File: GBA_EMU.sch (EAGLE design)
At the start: 83 parts, among them J1 USB-MINIB-5PIN, J2 AVR_SPI, SW1 LEFT, SW2 RIGHT, SW3 PWR_SWITCH, U1 MIC7221, U2 MICROCHIP_MCP1642B-ADJ, U4 LM4875, U5 Mic5365-2.8Y, U7 AZV321, X2 HEADPHONE

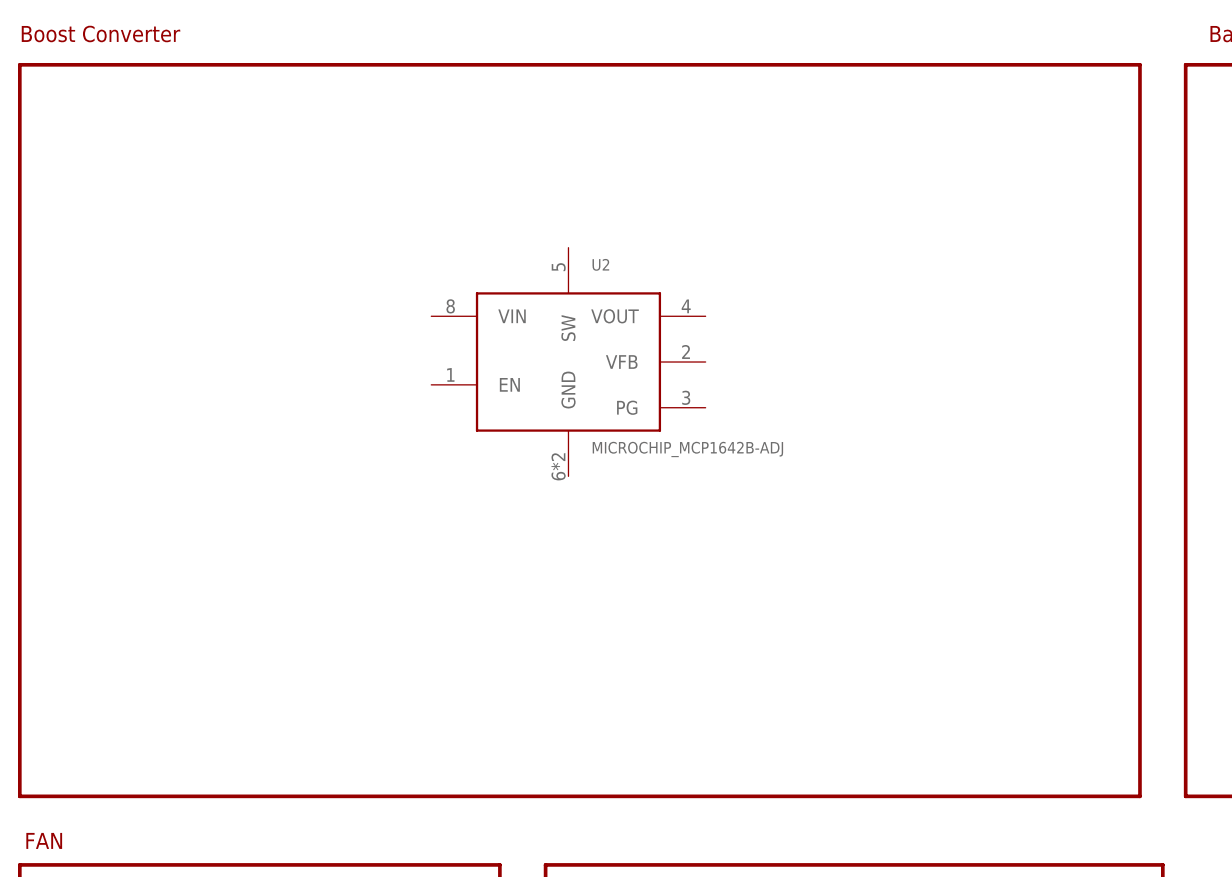
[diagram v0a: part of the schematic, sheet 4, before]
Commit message: added more to the power circuit
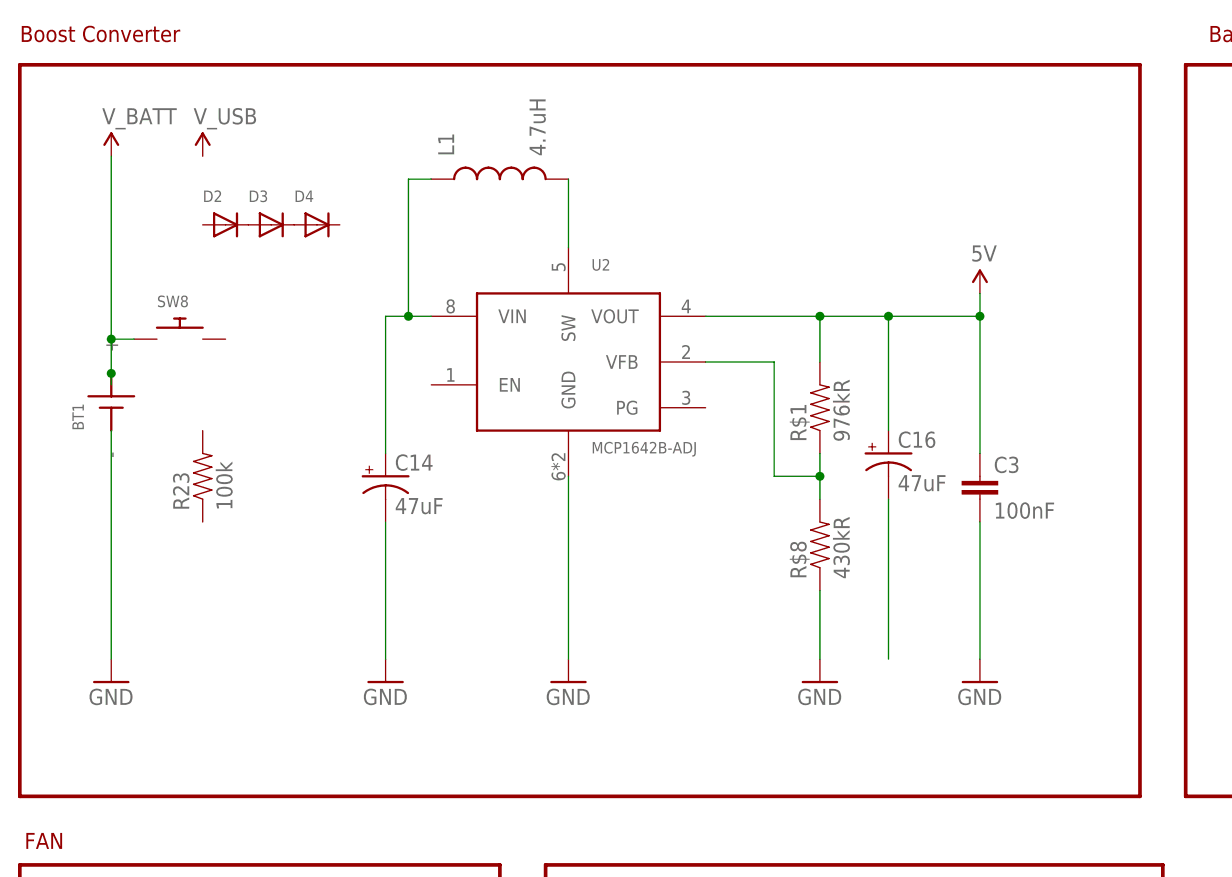
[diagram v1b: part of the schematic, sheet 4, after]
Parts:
- added BT1: (no value), custom:GBA_BATTERY
- added C14, C16: 47uF, SparkFun-Capacitors:47UF-10V-10%(TANT)
- added C3: 100nF, SparkFun-Capacitors:10PF-50V-5%(0603)
- added D2, D3, D4: (no value), adafruit:DIODESOD-523
- added L1: 4.7uH, SparkFun-Passives:INDUCTORINDUCTOR_4.7UH
- added R$1: 976kR, SparkFun-Resistors:820KOHM-1/10W-1%(0603)
- added R$8: 430kR, SparkFun-Resistors:820KOHM-1/10W-1%(0603)
- added R23: 100k, SparkFun-Resistors:100KOHM-1/10W-1%(0603)
- added SW8: (no value), adafruit:SWITCH_PUSHBUTTONSOFTTOUCHSMD_SJ
- added U$4: USB2523B, custom:USB2523B
- U2: value MICROCHIP_MCP1642B-ADJ -> MCP1642B-ADJ
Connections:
- new net N$23: R$1.1, R$8.2, U2.VFB
- new net N$30: C16.-
- new net N$31: D2.C, D3.A
- new net N$32: C14.+, L1.1, U2.VIN
- new net N$33: D3.C, D4.A
- new net N$34: L1.2, U2.SW
- net 5V: now also C16.+, C3.1, R$1.2, U2.VOUT
- net GND: now also BT1.-, C14.-, C3.2, R$8.1, U2.GND
- net V_BATT: now also BT1.+, SW8.P$1
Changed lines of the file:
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@@
 <part name="SUPPLY1" library="SparkFun-Aesthetics" deviceset="3.3V" device=""/>
 <part name="U1" library="custom" deviceset="SPARKFUN-ANALOGIC_MIC7221" device="" value="MIC7221"/>
-<part name="U2" library="custom" deviceset="MICROCHIP_MCP1642B-ADJ" device=""/>
+<part name="U2" library="custom" deviceset="MICROCHIP_MCP1642B-ADJ" device="" value="MCP1642B-ADJ"/>
 <part name="R3" library="SparkFun-Resistors" deviceset="100KOHM-1/10W-1%(0603)" device="" value="100k"/>
 <part name="R4" library="SparkFun-Resistors" deviceset="287OHM-1/10W-1%(0603)" device="" value="270"/>
@@
 <part name="R22" library="SparkFun-Resistors" deviceset="4.7KOHM-1/10W-1%(0603)" device="" value="4.7K"/>
 <part name="SUPPLY27" library="SparkFun-Aesthetics" deviceset="3.3V" device=""/>
+<part name="BT1" library="custom" deviceset="GBA_BATTERY" device=""/>
+<part name="SUPPLY28" library="SparkFun-Aesthetics" deviceset="V_BATT" device=""/>
+<part name="GND6" library="SparkFun-Aesthetics" deviceset="GND" device=""/>
+<part name="SUPPLY29" library="SparkFun-Aesthetics" deviceset="V_USB" device=""/>
+<part name="U$4" library="custom" deviceset="USB2523B" device=""/>
+<part name="GND15" library="SparkFun-Aesthetics" deviceset="GND" device=""/>
+<part name="C3" library="SparkFun-Capacitors" deviceset="10PF-50V-5%(0603)" device="" value="100nF"/>
+<part name="SUPPLY30" library="SparkFun-Aesthetics" deviceset="5V" device=""/>
+<part name="GND28" library="SparkFun-Aesthetics" deviceset="GND" device=""/>
+<part name="R$1" library="SparkFun-Resistors" deviceset="820KOHM-1/10W-1%(0603)" device="" value="976kR"/>
+<part name="R$8" library="SparkFun-Resistors" deviceset="820KOHM-1/10W-1%(0603)" device="" value="430kR"/>
+<part name="GND34" library="SparkFun-Aesthetics" deviceset="GND" device=""/>
+<part name="C14" library="SparkFun-Capacitors" deviceset="47UF-10V-10%(TANT)" device="" value="47uF"/>
+<part name="C16" library="SparkFun-Capacitors" deviceset="47UF-10V-10%(TANT)" device="" value="47uF"/>
+<part name="GND35" library="SparkFun-Aesthetics" deviceset="GND" device=""/>
+<part name="SW8" library="adafruit" deviceset="SWITCH_PUSHBUTTON" device="SOFTTOUCHSMD_SJ"/>
+<part name="D2" library="adafruit" deviceset="DIODE" device="SOD-523"/>
+<part name="R23" library="SparkFun-Resistors" deviceset="100KOHM-1/10W-1%(0603)" device="" value="100k"/>
+<part name="D3" library="adafruit" deviceset="DIODE" device="SOD-523"/>
+<part name="D4" library="adafruit" deviceset="DIODE" device="SOD-523"/>
+<part name="L1" library="SparkFun-Passives" deviceset="INDUCTOR" device="INDUCTOR_4.7UH" value="4.7uH"/>
 </parts>
 <sheets>
@@
 <instance part="TP6" gate="G$1" x="76.2" y="27.94"/>
 <instance part="TP7" gate="G$1" x="83.82" y="27.94"/>
+<instance part="U$4" gate="G$1" x="200.66" y="121.92"/>
 </instances>
 <busses>
@@
 <instance part="R12" gate="G$1" x="33.02" y="38.1" rot="R90"/>
 <instance part="U2" gate="U$1" x="53.34" y="121.92"/>
+<instance part="BT1" gate="BT$1" x="10.16" y="121.92" rot="R90"/>
+<instance part="SUPPLY28" gate="G$1" x="10.16" y="147.32"/>
+<instance part="GND6" gate="1" x="10.16" y="88.9"/>
+<instance part="SUPPLY29" gate="G$1" x="20.32" y="147.32"/>
+<instance part="GND15" gate="1" x="60.96" y="88.9"/>
+<instance part="C3" gate="G$1" x="106.68" y="109.22"/>
+<instance part="SUPPLY30" gate="G$1" x="106.68" y="132.08"/>
+<instance part="GND28" gate="1" x="106.68" y="88.9"/>
+<instance part="R$1" gate="G$1" x="88.9" y="119.38" rot="R90"/>
+<instance part="R$8" gate="G$1" x="88.9" y="104.14" rot="R90"/>
+<instance part="GND34" gate="1" x="88.9" y="88.9"/>
+<instance part="C14" gate="G$1" x="40.64" y="111.76"/>
+<instance part="C16" gate="G$1" x="96.52" y="114.3"/>
+<instance part="GND35" gate="1" x="40.64" y="88.9"/>
+<instance part="SW8" gate="G$1" x="17.78" y="127"/>
+<instance part="D2" gate="G$1" x="22.86" y="139.7"/>
+<instance part="R23" gate="G$1" x="20.32" y="111.76" rot="R90"/>
+<instance part="D3" gate="G$1" x="27.94" y="139.7"/>
+<instance part="D4" gate="G$1" x="33.02" y="139.7"/>
+<instance part="L1" gate="G$1" x="53.34" y="144.78" rot="R90"/>
 </instances>
 <busses>
@@
 <wire x1="20.32" y1="25.4" x2="20.32" y2="15.24" width="0.1524" layer="91"/>
 </segment>
+<segment>
+<pinref part="BT1" gate="BT$1" pin="-"/>
+<pinref part="GND6" gate="1" pin="GND"/>
+<wire x1="10.16" y1="116.84" x2="10.16" y2="91.44" width="0.1524" layer="91"/>
+</segment>
+<segment>
+<pinref part="GND15" gate="1" pin="GND"/>
+<pinref part="U2" gate="U$1" pin="GND"/>
+<wire x1="60.96" y1="91.44" x2="60.96" y2="111.76" width="0.1524" layer="91"/>
+</segment>
+<segment>
+<pinref part="C3" gate="G$1" pin="2"/>
+<pinref part="GND28" gate="1" pin="GND"/>
+<wire x1="106.68" y1="106.68" x2="106.68" y2="91.44" width="0.1524" layer="91"/>
+</segment>
+<segment>
+<pinref part="R$8" gate="G$1" pin="1"/>
+<pinref part="GND34" gate="1" pin="GND"/>
+<wire x1="88.9" y1="99.06" x2="88.9" y2="91.44" width="0.1524" layer="91"/>
+</segment>
+<segment>
+<pinref part="C14" gate="G$1" pin="-"/>
+<pinref part="GND35" gate="1" pin="GND"/>
+<wire x1="40.64" y1="106.68" x2="40.64" y2="91.44" width="0.1524" layer="91"/>
+</segment>
 </net>
 <net name="5V" class="0">
@@
 <wire x1="22.86" y1="40.64" x2="17.78" y2="40.64" width="0.1524" layer="91"/>
 </segment>
+<segment>
+<pinref part="SUPPLY30" gate="G$1" pin="5V"/>
+<pinref part="C3" gate="G$1" pin="1"/>
+<wire x1="106.68" y1="132.08" x2="106.68" y2="129.54" width="0.1524" layer="91"/>
+<pinref part="U2" gate="U$1" pin="VOUT"/>
+<wire x1="106.68" y1="129.54" x2="106.68" y2="114.3" width="0.1524" layer="91"/>
+<wire x1="76.2" y1="129.54" x2="88.9" y2="129.54" width="0.1524" layer="91"/>
+<junction x="106.68" y="129.54"/>
+<pinref part="R$1" gate="G$1" pin="2"/>
+<wire x1="88.9" y1="129.54" x2="96.52" y2="129.54" width="0.1524" layer="91"/>
+<wire x1="96.52" y1="129.54" x2="106.68" y2="129.54" width="0.1524" layer="91"/>
+<wire x1="88.9" y1="124.46" x2="88.9" y2="129.54" width="0.1524" layer="91"/>
+<junction x="88.9" y="129.54"/>
+<pinref part="C16" gate="G$1" pin="+"/>
+<wire x1="96.52" y1="116.84" x2="96.52" y2="129.54" width="0.1524" layer="91"/>
+<junction x="96.52" y="129.54"/>
+</segment>
 </net>
 <net name="N$39" class="0">
@@
 </segment>
 </net>
+<net name="V_BATT" class="0">
+<segment>
+<pinref part="SUPPLY28" gate="G$1" pin="V_BATT"/>
+<wire x1="10.16" y1="121.92" x2="10.16" y2="123.19" width="0.1524" layer="91"/>
+<pinref part="BT1" gate="BT$1" pin="+"/>
+<wire x1="10.16" y1="123.19" x2="10.16" y2="127" width="0.1524" layer="91"/>
+<junction x="10.16" y="123.19"/>
+<pinref part="SW8" gate="G$1" pin="P$1"/>
+<wire x1="10.16" y1="127" x2="10.16" y2="147.32" width="0.1524" layer="91"/>
+<wire x1="12.7" y1="127" x2="10.16" y2="127" width="0.1524" layer="91"/>
+<junction x="10.16" y="127"/>
+</segment>
+</net>
+<net name="N$23" class="0">
+<segment>
+<pinref part="U2" gate="U$1" pin="VFB"/>
+<wire x1="76.2" y1="124.46" x2="83.82" y2="124.46" width="0.1524" layer="91"/>
+<wire x1="83.82" y1="124.46" x2="83.82" y2="111.76" width="0.1524" layer="91"/>
+<wire x1="83.82" y1="111.76" x2="88.9" y2="111.76" width="0.1524" layer="91"/>
+<pinref part="R$1" gate="G$1" pin="1"/>
+<wire x1="88.9" y1="111.76" x2="88.9" y2="114.3" width="0.1524" layer="91"/>
+<pinref part="R$8" gate="G$1" pin="2"/>
+<wire x1="88.9" y1="111.76" x2="88.9" y2="109.22" width="0.1524" layer="91"/>
+<junction x="88.9" y="111.76"/>
+</segment>
+</net>
+<net name="N$30" class="0">
+<segment>
+<pinref part="C16" gate="G$1" pin="-"/>
+<wire x1="96.52" y1="109.22" x2="96.52" y2="91.44" width="0.1524" layer="91"/>
+</segment>
+</net>
+<net name="N$32" class="0">
+<segment>
+<pinref part="U2" gate="U$1" pin="VIN"/>
+<wire x1="45.72" y1="129.54" x2="43.18" y2="129.54" width="0.1524" layer="91"/>
+<pinref part="C14" gate="G$1" pin="+"/>
+<wire x1="43.18" y1="129.54" x2="40.64" y2="129.54" width="0.1524" layer="91"/>
+<wire x1="40.64" y1="114.3" x2="40.64" y2="129.54" width="0.1524" layer="91"/>
+<pinref part="L1" gate="G$1" pin="1"/>
+<wire x1="45.72" y1="144.78" x2="43.18" y2="144.78" width="0.1524" layer="91"/>
+<wire x1="43.18" y1="144.78" x2="43.18" y2="129.54" width="0.1524" layer="91"/>
+<junction x="43.18" y="129.54"/>
+</segment>
+</net>
+<net name="N$31" class="0">
+<segment>
+<pinref part="D2" gate="G$1" pin="C"/>
+<pinref part="D3" gate="G$1" pin="A"/>
+</segment>
+</net>
+<net name="N$33" class="0">
+<segment>
+<pinref part="D3" gate="G$1" pin="C"/>
+<pinref part="D4" gate="G$1" pin="A"/>
+</segment>
+</net>
+<net name="N$34" class="0">
+<segment>
+<pinref part="U2" gate="U$1" pin="SW"/>
+<pinref part="L1" gate="G$1" pin="2"/>
+<wire x1="60.96" y1="137.16" x2="60.96" y2="144.78" width="0.1524" layer="91"/>
+</segment>
+</net>

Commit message: moved all buttons to pi instead of copro
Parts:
- removed U$4: USB2523B, custom:USB2523B
- added D5, D6: DIODE_DFLS130L, custom:DIODE_DFLS130L
- added X1: (no value), Adafruit_PowerBoost:MICROBUILDER_USB_TYPEAPTHFML
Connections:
- removed net DOWN: COPRO.PD1(INT1/AIN0), DOWN.2
- removed net LEFT: COPRO.PC6(OC1A/PCINT8), LEFT.2
- removed net LEFT_BUMP: SW1.2
- removed net PI_DC: U$1.2A4
- removed net PWM0: R8.1
- removed net RIGHT: COPRO.PC7(ICP1/INT4/CLKO), RIGHT.2
- removed net RIGHT_BUMP: SW2.2
- removed net SELECT: COPRO.PD7(INT7/HWB/AIN6/T0), SEL.2
- removed net START: COPRO.PD6(INT6/AIN5/RTS), START.2
- removed net UP: COPRO.PD0(INT0/OC0B), UP.2
- new net DOWN_BTN: DOWN.2, PCB1.59/GPIO17
- new net L1_BTN: PCB1.21/GPIO6, SW1.2
- new net LEFT_BTN: LEFT.2, PCB1.89/GPIO27
- new net N$35: PCB1.177/RUN
- new net N$36: PCB1.197/VBAT, PCB1.199/VBAT
- new net N$37: PCB1.198/VBAT, PCB1.200/VBAT
- new net PI_PWM0: PCB1.63/GPIO18, R8.1
- new net PI_TFT_DC: PCB1.11/GPIO3, U$1.2A4
- new net PWR_EN: COPRO.PD0(INT0/OC0B), U2.EN
- new net R1_BTN: PCB1.71/GPIO21, SW2.2
- new net RIGHT_BTN: PCB1.75/GPIO22, RIGHT.2
- new net SELECT_BTN: PCB1.81/GPIO24, SEL.2
- new net START_BTN: PCB1.77/GPIO23, START.2
- new net UP_BTN: PCB1.17/GPIO5, UP.2
- net 1.8V: now also TP5.TP
- net 3.3V: now also PCB1.40/GPIO0-27_VREF
- net 5V: now also X1.VBUS
- net A_BTN: now also PCB1.65/GPIO19; no longer COPRO.PD4(INT5/AIN3)
- net B_BTN: now also PCB1.87/GPIO26; no longer COPRO.PD5(XCK/AIN4/PCINT12)
- net GND: now also C16.-, X1.GND
- net L2_BTN: now also PCB1.57/GPIO16; no longer COPRO.PC4(PCINT10)
- net N$12: now also D5.C, D6.C, SW8.P$1; no longer SW3.O
- net N$30: now also PCB1.179/VDD_CORE; no longer C16.-
- net N$32: now also SW8.P$2
- net PI_MOSI: now also PCB1.33/GPIO10
- net PI_SCK: now also PCB1.35/GPIO11
- net PI_TFT_RESET: now also PCB1.9/GPIO2
- net R2_BTN: now also PCB1.45/GPIO12; no longer COPRO.PC5(OC1B/PCINT9)
- net TFT_CS: now also COPRO.PD4(INT5/AIN3)
- net TFT_LED: now also PCB1.15/GPIO4
- net V_BATT: now also D6.A; no longer SW8.P$1
- net V_USB: now also D5.A
- net X_BTN: now also PCB1.83/GPIO25; no longer COPRO.PB7(OC0A/OC1C/PCINT7)
- net Y_BTN: no longer COPRO.PC2(AIN2/PCIN11)
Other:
- note added: "C16 as close to VOUT as possible"
- note added: "Power Or'ing"
- note removed: "Place C10 as close as possible to Vout on U3."
- moved on the sheet: D2, D3, D4, J1, POT1SW, R16, R21, R22, R23, R8, SW8
